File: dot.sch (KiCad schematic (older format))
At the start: 36 parts, among them J1 PWR, J2 GPIO, J4 USB_C_Receptacle_USB2.0, Q1 SQM40031EL, Q2 MMBT2222, Q3 MMBT2222, SW1 SW_Push, U1 ESP32-WROOM-32D, U2 ADP2108AUJ-3.3, U3 CH340T

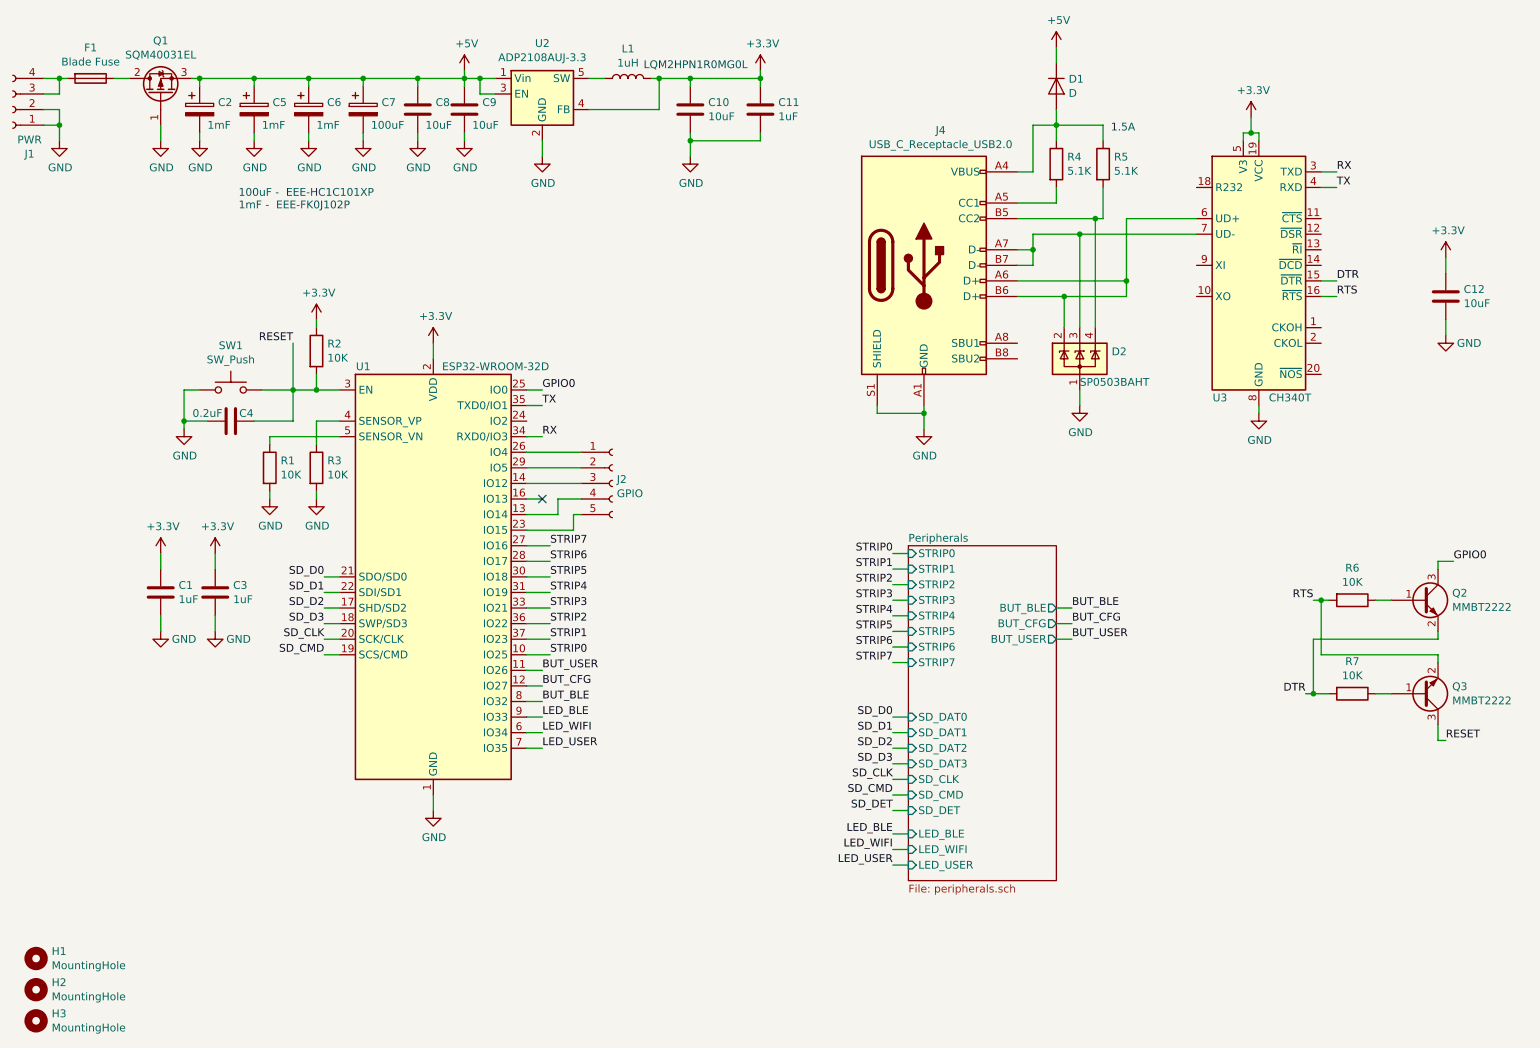
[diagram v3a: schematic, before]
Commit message: Updated schematic to use right footprint, change fuse holder, and removal of caps
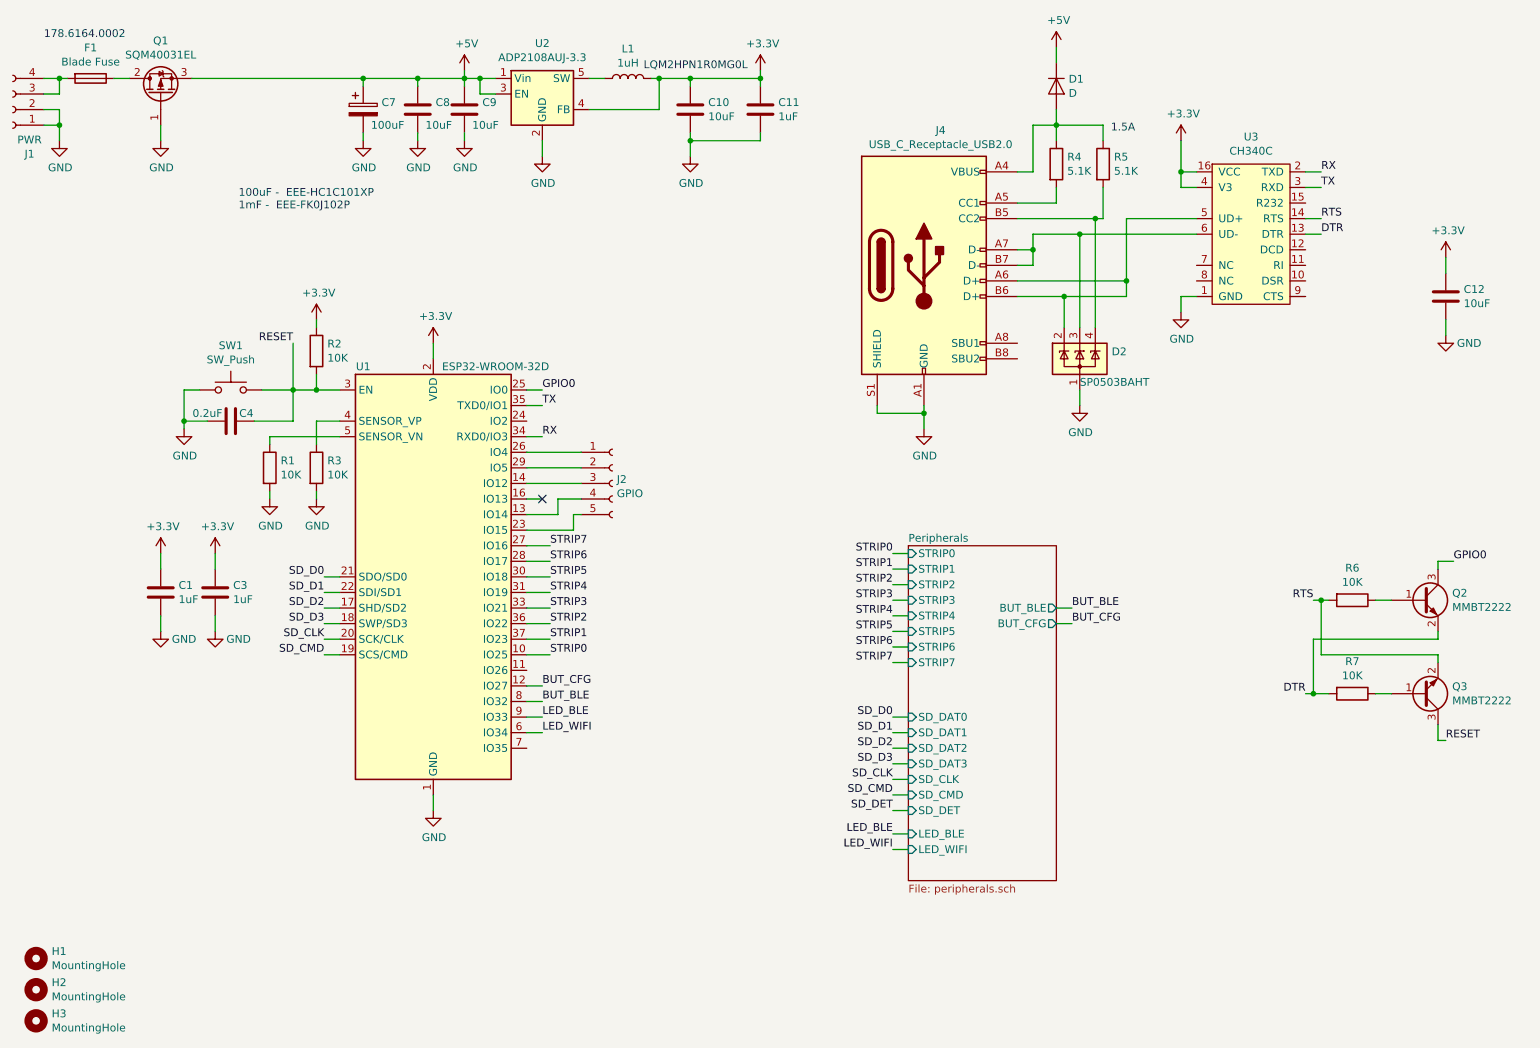
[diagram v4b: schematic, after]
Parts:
- removed C2, C5, C6: 1mF, Capacitor_SMD:CP_Elec_8x10.5, symbol Device:CP
- removed U3: CH340T, Package_SO:SSOP-20_5.3x7.2mm_P0.65mm, symbol Interface_USB:CH340T
- added U3: CH340C, Package_SO:SOP-16_4.4x10.4mm_P1.27mm, symbol dot:CH340C
- F1: footprint Fuse:Fuseholder_Blade_Mini_Keystone_3568 -> Fuse:Fuseholder_Blade_ATO_Littelfuse_Pudenz_2_Pin
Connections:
- net +3V3: now also U3.16 (VCC), U3.4 (V3)
- net DTR: now also U3.13 (DTR)
- net GND: now also U3.1 (GND)
- net RTS: now also U3.14 (RTS)
- net RX: now also U3.2 (TXD)
- net TX: now also U3.3 (RXD)
- net at D2.2 (K), J4.A6 (D+), J4.B6 (D+): now also U3.5 (UD+)
- net at D2.3 (K), J4.A7 (D-), J4.B7 (D-): now also U3.6 (UD-)
- net BUT_USER: no longer names the net of U1.11 (IO26)
- net LED_USER: no longer names the net of U1.7 (IO35)
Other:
- note added: "178.6164.0002"
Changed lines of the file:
@@
 	1800 1550 1800 1450
-$Comp
-L Device:CP C5
-U 1 1 5DF6CE11
-P 2400 1350
-F 0 "C5" H 2518 1396 50  0000 L CNN
-F 1 "1mF" H 2450 1250 50  0000 L CNN
-F 2 "Capacitor_SMD:CP_Elec_8x10.5" H 2438 1200 50  0001 C CNN
-F 3 "~" H 2400 1350 50  0001 C CNN
-	1    2400 1350
-	1    0    0    -1
-$EndComp
-$Comp
-L Device:CP C6
-U 1 1 5DF6FAD9
-P 2750 1350
-F 0 "C6" H 2868 1396 50  0000 L CNN
-F 1 "1mF" H 2800 1250 50  0000 L CNN
-F 2 "Capacitor_SMD:CP_Elec_8x10.5" H 2788 1200 50  0001 C CNN
-F 3 "~" H 2750 1350 50  0001 C CNN
-	1    2750 1350
-	1    0    0    -1
-$EndComp
-$Comp
-L Device:CP C2
-U 1 1 5DF70D2F
-P 2050 1350
-F 0 "C2" H 2168 1396 50  0000 L CNN
-F 1 "1mF" H 2100 1250 50  0000 L CNN
-F 2 "Capacitor_SMD:CP_Elec_8x10.5" H 2088 1200 50  0001 C CNN
-F 3 "~" H 2050 1350 50  0001 C CNN
-	1    2050 1350
-	1    0    0    -1
-$EndComp
-Wire Wire Line
-	2750 1200 2750 1150
-Wire Wire Line
-	2750 1150 2400 1150
-Wire Wire Line
-	2050 1200 2050 1150
-Connection ~ 2050 1150
-Wire Wire Line
-	2050 1150 2000 1150
-Wire Wire Line
-	2400 1200 2400 1150
-Connection ~ 2400 1150
-Wire Wire Line
-	2400 1150 2050 1150
-$Comp
-L power:GND #PWR0103
-U 1 1 5DF88C4C
-P 2050 1550
-F 0 "#PWR0103" H 2050 1300 50  0001 C CNN
-F 1 "GND" H 2055 1377 50  0000 C CNN
-F 2 "" H 2050 1550 50  0001 C CNN
-F 3 "" H 2050 1550 50  0001 C CNN
-	1    2050 1550
-	1    0    0    -1
-$EndComp
-$Comp
-L power:GND #PWR0104
-U 1 1 5DF88F6E
-P 2400 1550
-F 0 "#PWR0104" H 2400 1300 50  0001 C CNN
-F 1 "GND" H 2405 1377 50  0000 C CNN
-F 2 "" H 2400 1550 50  0001 C CNN
-F 3 "" H 2400 1550 50  0001 C CNN
-	1    2400 1550
-	1    0    0    -1
-$EndComp
-$Comp
-L power:GND #PWR0105
-U 1 1 5DF892B8
-P 2750 1550
-F 0 "#PWR0105" H 2750 1300 50  0001 C CNN
-F 1 "GND" H 2755 1377 50  0000 C CNN
-F 2 "" H 2750 1550 50  0001 C CNN
-F 3 "" H 2750 1550 50  0001 C CNN
-	1    2750 1550
-	1    0    0    -1
-$EndComp
-Wire Wire Line
-	2750 1500 2750 1550
-Wire Wire Line
-	2400 1500 2400 1550
-Wire Wire Line
-	2050 1500 2050 1550
 $Comp
 L Device:C C8
@@
 Wire Wire Line
 	3450 1150 3100 1150
-Connection ~ 2750 1150
 $Comp
 L Device:C C9
@@
 F2 "LED_BLE" I L 6600 6000 50
 F3 "LED_WIFI" I L 6600 6100 50
-F4 "LED_USER" I L 6600 6200 50
-F5 "STRIP0" I L 6600 4200 50
-F6 "STRIP1" I L 6600 4300 50
-F7 "STRIP2" I L 6600 4400 50
-F8 "SD_DAT2" I L 6600 5450 50
-F9 "SD_DAT3" I L 6600 5550 50
-F10 "SD_CMD" I L 6600 5750 50
-F11 "SD_CLK" I L 6600 5650 50
-F12 "SD_DAT0" I L 6600 5250 50
-F13 "SD_DAT1" I L 6600 5350 50
-F14 "SD_DET" I L 6600 5850 50
-F15 "BUT_BLE" O R 7550 4550 50
-F16 "BUT_CFG" O R 7550 4650 50
-F17 "BUT_USER" O R 7550 4750 50
-F18 "STRIP3" I L 6600 4500 50
-F19 "STRIP4" I L 6600 4600 50
-F20 "STRIP5" I L 6600 4700 50
-F21 "STRIP6" I L 6600 4800 50
-F22 "STRIP7" I L 6600 4900 50
+F4 "STRIP0" I L 6600 4200 50
+F5 "STRIP1" I L 6600 4300 50
+F6 "STRIP2" I L 6600 4400 50
+F7 "SD_DAT2" I L 6600 5450 50
+F8 "SD_DAT3" I L 6600 5550 50
+F9 "SD_CMD" I L 6600 5750 50
+F10 "SD_CLK" I L 6600 5650 50
+F11 "SD_DAT0" I L 6600 5250 50
+F12 "SD_DAT1" I L 6600 5350 50
+F13 "SD_DET" I L 6600 5850 50
+F14 "BUT_BLE" O R 7550 4550 50
+F15 "BUT_CFG" O R 7550 4650 50
+F16 "STRIP3" I L 6600 4500 50
+F17 "STRIP4" I L 6600 4600 50
+F18 "STRIP5" I L 6600 4700 50
+F19 "STRIP6" I L 6600 4800 50
+F20 "STRIP7" I L 6600 4900 50
 $EndSheet
 $Comp
@@
 	1    0    0    -1
 $EndComp
-$Comp
-L Device:CP C7
-U 1 1 5E227B1D
-P 3100 1350
-F 0 "C7" H 3218 1396 50  0000 L CNN
-F 1 "100uF" H 3150 1250 50  0000 L CNN
-F 2 "Capacitor_SMD:CP_Elec_6.3x3.9" H 3138 1200 50  0001 C CNN
-F 3 "~" H 3100 1350 50  0001 C CNN
-	1    3100 1350
-	1    0    0    -1
-$EndComp
 Wire Wire Line
 	3100 1500 3100 1550
@@
 	3100 1200 3100 1150
 Connection ~ 3100 1150
-Wire Wire Line
-	3100 1150 2750 1150
 $Comp
 L power:GND #PWR0123
@@
 L power:+3.3V #PWR0124
 U 1 1 5E1AD7A0
-P 8800 1400
-F 0 "#PWR0124" H 8800 1250 50  0001 C CNN
-F 1 "+3.3V" H 8815 1573 50  0000 C CNN
-F 2 "" H 8800 1400 50  0001 C CNN
-F 3 "" H 8800 1400 50  0001 C CNN
-	1    8800 1400
+P 8350 1550
+F 0 "#PWR0124" H 8350 1400 50  0001 C CNN
+F 1 "+3.3V" H 8365 1723 50  0000 C CNN
+F 2 "" H 8350 1550 50  0001 C CNN
+F 3 "" H 8350 1550 50  0001 C CNN
+	1    8350 1550
 	1    0    0    -1
 $EndComp
@@
 L power:GND #PWR0125
 U 1 1 5E1A1A9F
-P 8850 3300
-F 0 "#PWR0125" H 8850 3050 50  0001 C CNN
-F 1 "GND" H 8855 3127 50  0000 C CNN
-F 2 "" H 8850 3300 50  0001 C CNN
-F 3 "" H 8850 3300 50  0001 C CNN
-	1    8850 3300
+P 8350 2650
+F 0 "#PWR0125" H 8350 2400 50  0001 C CNN
+F 1 "GND" H 8355 2477 50  0000 C CNN
+F 2 "" H 8350 2650 50  0001 C CNN
+F 3 "" H 8350 2650 50  0001 C CNN
+	1    8350 2650
 	1    0    0    -1
 $EndComp
@@
 F 0 "F1" V 1153 1150 50  0000 C CNN
 F 1 "Blade Fuse" V 1244 1150 50  0000 C CNN
-F 2 "Fuse:Fuseholder_Blade_Mini_Keystone_3568" V 1280 1150 50  0001 C CNN
+F 2 "Fuse:Fuseholder_Blade_ATO_Littelfuse_Pudenz_2_Pin" V 1280 1150 50  0001 C CNN
 F 3 "~" H 1350 1150 50  0001 C CNN
 	1    1350 1150
@@
 BUT_CFG
 Wire Wire Line
-	7650 4750 7550 4750
-Text Label 7650 4750 0    50   ~ 0
-BUT_USER
-Wire Wire Line
 	6600 4200 6500 4200
 Wire Wire Line
@@
 Wire Wire Line
 	6500 6100 6600 6100
-Wire Wire Line
-	6500 6200 6600 6200
 Text Label 6500 6000 2    50   ~ 0
 LED_BLE
 Text Label 6500 6100 2    50   ~ 0
 LED_WIFI
-Text Label 6500 6200 2    50   ~ 0
-LED_USER
-Wire Wire Line
-	4250 5450 4150 5450
 Wire Wire Line
 	4250 5350 4150 5350
@@
 Wire Wire Line
 	4250 5050 4150 5050
-Wire Wire Line
-	4250 4950 4150 4950
-Text Label 4250 4950 0    50   ~ 0
-BUT_USER
 Text Label 4250 5050 0    50   ~ 0
 BUT_CFG
@@
 Text Label 4250 5350 0    50   ~ 0
 LED_WIFI
-Text Label 4250 5450 0    50   ~ 0
-LED_USER
 Text Label 6500 4500 2    50   ~ 0
 STRIP3
@@
 Wire Wire Line
 	6600 4600 6500 4600
-$Comp
-L Interface_USB:CH340T U3
-U 1 1 5E2FA337
-P 8850 2450
-F 0 "U3" H 8600 1700 50  0000 C CNN
-F 1 "CH340T" H 9050 1700 50  0000 C CNN
-F 2 "Package_SO:SSOP-20_5.3x7.2mm_P0.65mm" H 9750 1650 50  0001 C CNN
-F 3 "https://cdn.sparkfun.com/datasheets/Dev/Arduino/Other/CH340DS1.PDF" H 8600 3300 50  0001 C CNN
-	1    8850 2450
-	1    0    0    -1
-$EndComp
 Wire Wire Line
 	7400 2250 7400 2150
@@
 	8000 2050 8000 2450
 Wire Wire Line
-	8850 3300 8850 3250
-Wire Wire Line
-	8800 1400 8800 1500
-Wire Wire Line
-	8800 1500 8750 1500
-Wire Wire Line
-	8750 1500 8750 1550
-Wire Wire Line
-	8800 1500 8850 1500
-Wire Wire Line
-	8850 1500 8850 1550
-Connection ~ 8800 1500
-Wire Wire Line
-	9350 1850 9250 1850
-Wire Wire Line
-	9350 1750 9250 1750
-Text Label 9350 1750 0    50   ~ 0
+	9250 1850 9150 1850
+Wire Wire Line
+	9250 1750 9150 1750
+Text Label 9250 1750 0    50   ~ 0
 RX
-Text Label 9350 1850 0    50   ~ 0
+Text Label 9250 1850 0    50   ~ 0
 TX
 Wire Wire Line
-	9350 2550 9250 2550
-Text Label 9350 2550 0    50   ~ 0
+	9250 2050 9150 2050
+Text Label 9250 2050 0    50   ~ 0
 RTS
 Wire Wire Line
-	9350 2450 9250 2450
-Text Label 9350 2450 0    50   ~ 0
+	9250 2150 9150 2150
+Text Label 9250 2150 0    50   ~ 0
 DTR
+$Comp
+L Device:CP C7
+U 1 1 5E227B1D
+P 3100 1350
+F 0 "C7" H 3218 1396 50  0000 L CNN
+F 1 "100uF" H 3150 1250 50  0000 L CNN
+F 2 "Capacitor_SMD:CP_Elec_6.3x3.9" H 3138 1200 50  0001 C CNN
+F 3 "~" H 3100 1350 50  0001 C CNN
+	1    3100 1350
+	1    0    0    -1
+$EndComp
+$Comp
+L dot:CH340C U3
+U 1 1 5E8238C1
+P 8800 2600
+F 0 "U3" H 8800 3675 50  0000 C CNN
+F 1 "CH340C" H 8800 3584 50  0000 C CNN
+F 2 "Package_SO:SOP-16_4.4x10.4mm_P1.27mm" H 8750 2500 50  0001 C CNN
+F 3 "" H 8750 2500 50  0001 C CNN
+	1    8800 2600
+	1    0    0    -1
+$EndComp
+Wire Wire Line
+	8450 2550 8350 2550
+Wire Wire Line
+	8350 2550 8350 2650
+Wire Wire Line
+	8350 1850 8450 1850
+Wire Wire Line
+	8350 1550 8350 1750
+Wire Wire Line
+	8450 1750 8350 1750
+Connection ~ 8350 1750
+Wire Wire Line
+	8350 1750 8350 1850
+Wire Wire Line
+	2000 1150 3100 1150
+Text Notes 1050 900  0    50   ~ 0
+178.6164.0002
 $EndSCHEMATC
